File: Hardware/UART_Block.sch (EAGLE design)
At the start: 27 parts, among them U4 TPS62065

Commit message: added DCIN pin added DCIN enable circuit corrected Copper pours corrected name changed names of board and SCH replaced power button updated header footprint added units and cleaned up dimensions
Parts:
- removed R6, R7: 100, SparkFun-Resistors:100OHM1/10W1%(0603)
- added Q1: BSS138, SparkFun-DiscreteSemi:MOSFET-NCHANNELBSS138
- added R15: 1K, SparkFun-Resistors:1KOHM1/10W1%(0603)
- added S2: DPDT, SparkFun-Electromechanical:SWITCH-DPDTAYZ0202
- S1: device SparkFun-Electromechanical:SWITCH-MOMENTARY-2-SMD-1101NE -> SparkFun-Electromechanical:SWITCH-MOMENTARY-2TACTILE-SWITCH-SMD-RIGHT-ANGLE
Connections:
- removed net N$3: R7.1, U1.A1
- removed net N$4: R6.1, U1.A2
- new net DCIN: E1.DCIN, Q1.S, U$3.DCIN
- new net N$1: Q1.G, R15.1
- new net UART1RX: S2.6, U1.B4
- new net UART1TX: S2.3, U1.B3
- new net UART2RX: S2.4, U1.B2
- new net UART2TX: S2.1, U1.B1
- net GND: now also JP2.5, JP2.6; no longer JP2.1, JP2.2
- net GP130_UART_1_RX: now also U1.A4
- net GP131_UART_1_TX: now also U1.A3
- net GP134_UART_2_RX: now also U1.A2; no longer R6.2
- net GP135_UART_2_TX: now also U1.A1; no longer R7.2
- net RXD: now also JP2.2, S2.2; no longer JP2.5, U1.B1
- net TXD: now also JP2.3, S2.5; no longer JP2.4, U1.B2
- net VCC: now also JP2.4, R15.2; no longer JP2.3
- net VSYS: now also Q1.D
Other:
- note added: "Casey Kuhns"
- note added: "DCIN Enable Circuit Prevents Battery board from enabling DCIN"
- note added: "v02"
- moved on the sheet: C1, C10, C2, C8, C9, D3, JP2, L1, R13, R14, R5, R8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

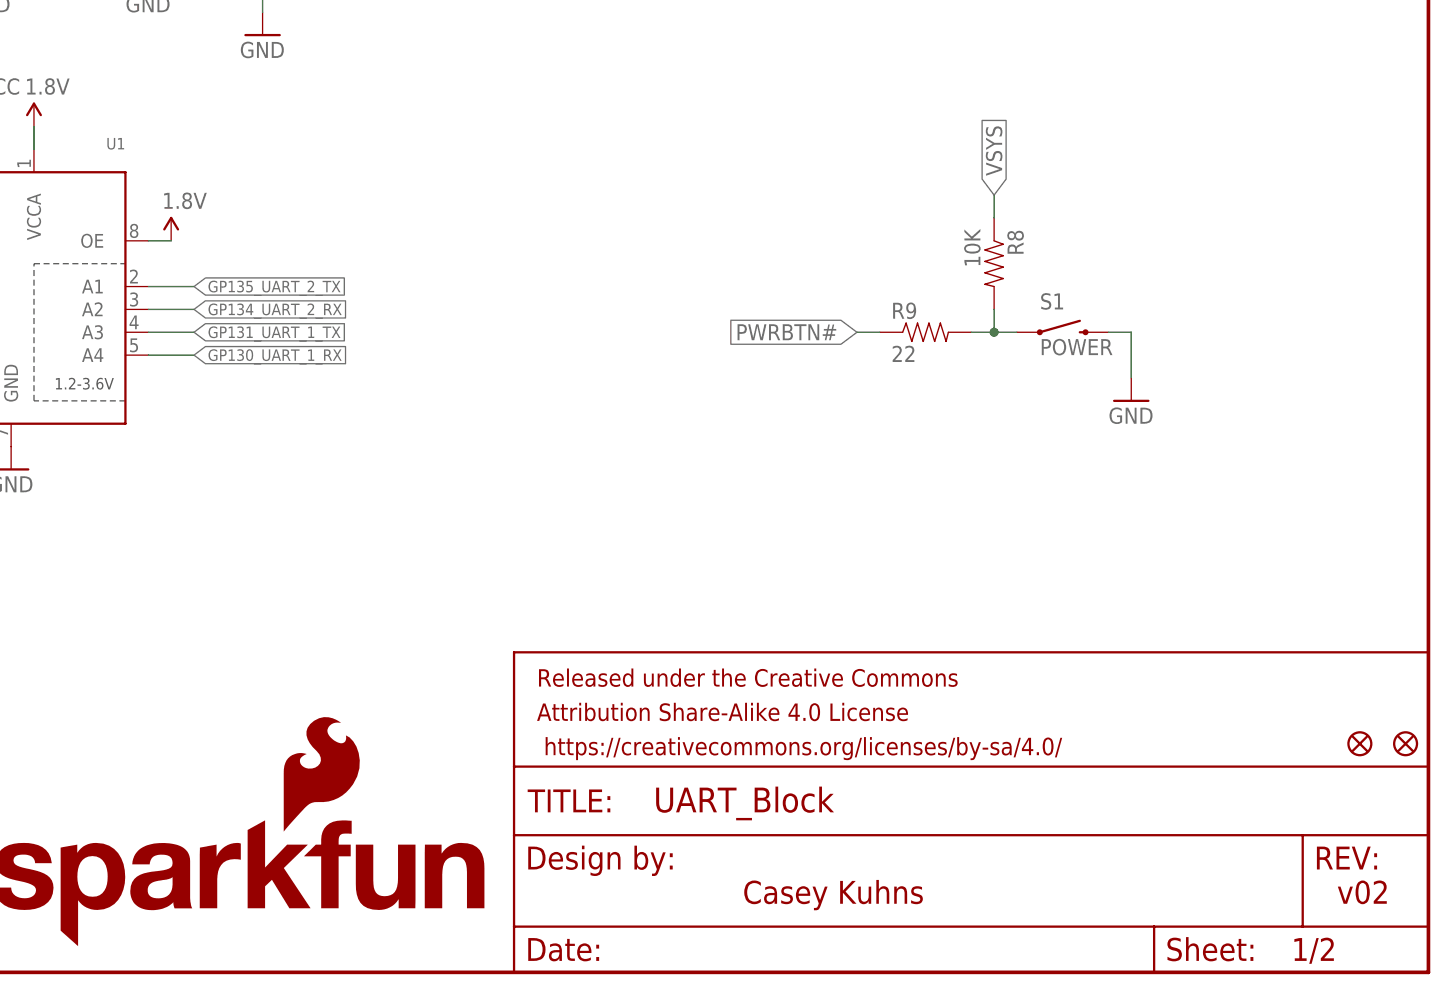
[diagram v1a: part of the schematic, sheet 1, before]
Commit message: Rev to 10, fix gnd, pwr, txt
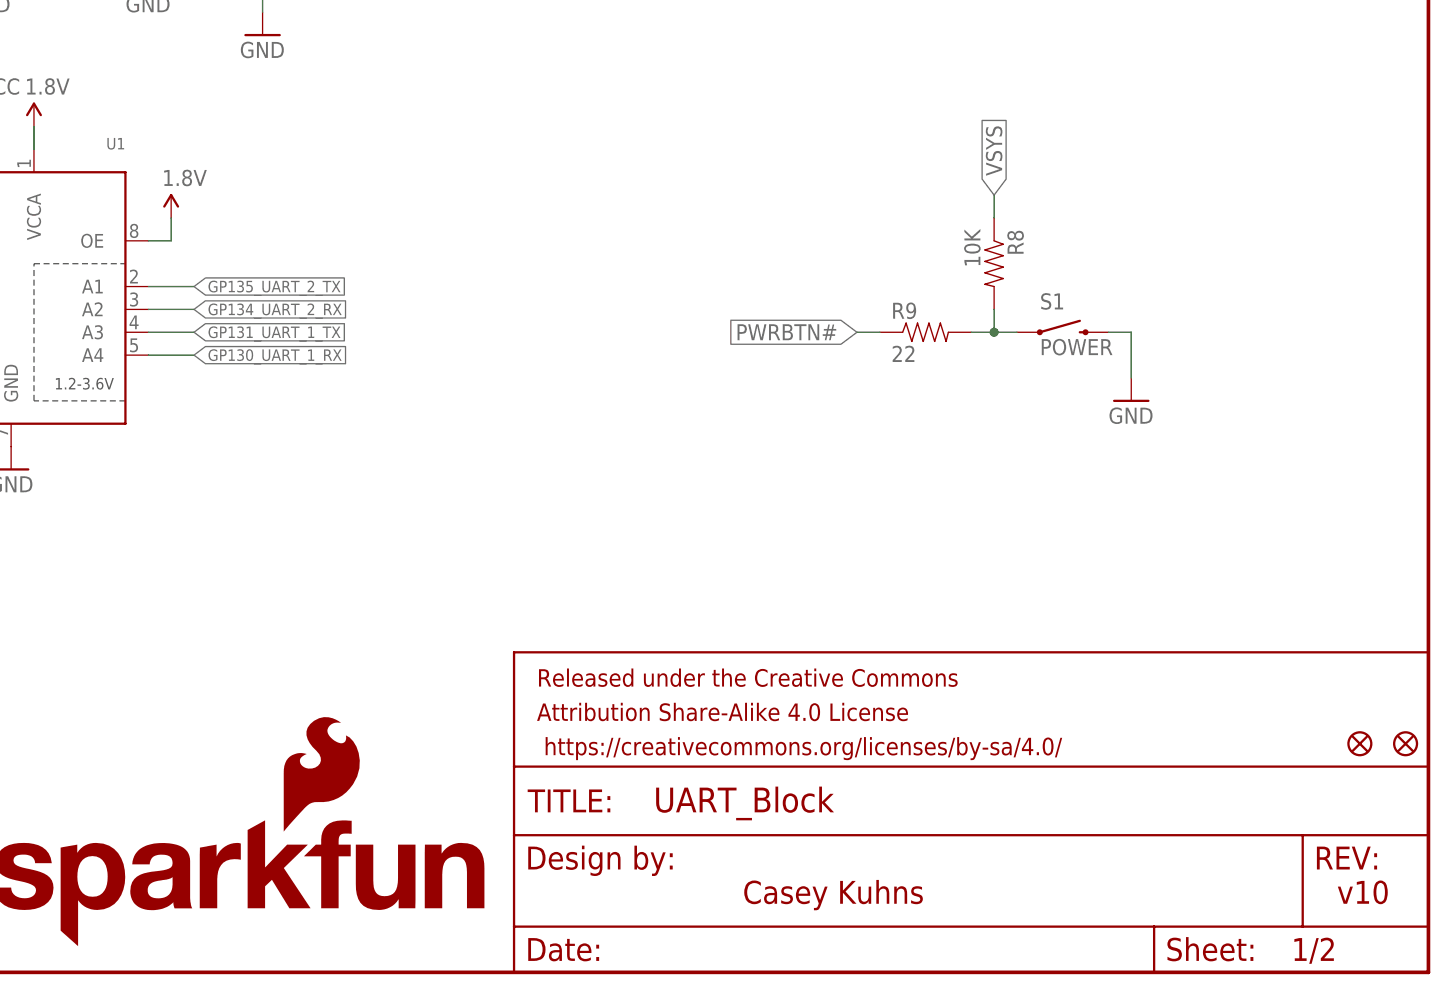
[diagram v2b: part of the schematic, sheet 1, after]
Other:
- note added: "v10"
- note removed: "v02"
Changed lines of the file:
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@@
 <?xml version="1.0" encoding="utf-8"?>
 <!DOCTYPE eagle SYSTEM "eagle.dtd">
-<eagle version="6.5.0">
+<eagle version="6.6.0">
 <drawing>
 <settings>
@@
 <layer number="255" name="routoute" color="7" fill="1" visible="no" active="yes"/>
 </layers>
-<schematic xreflabel="%F%N/%S.%C%R" xrefpart="/%S.%C%R">
+<schematic xreflabel="%F%N/%S" xrefpart="/%S.%C%R">
 <attributes>
 </attributes>
@@
 <text x="35.56" y="78.74" size="1.778" layer="94">Black</text>
 <text x="35.56" y="60.96" size="1.778" layer="94">Green</text>
-<text x="238.76" y="7.62" size="2.54" layer="94">v02</text>
+<text x="238.76" y="7.62" size="2.54" layer="94">v10</text>
 <text x="172.72" y="7.62" size="2.54" layer="94">Casey Kuhns</text>
 <text x="175.26" y="139.7" size="1.27" layer="97">DCIN Enable Circuit
@@
 <instance part="SUPPLY6" gate="G$1" x="20.32" y="76.2"/>
 <instance part="SUPPLY7" gate="G$1" x="22.86" y="137.16"/>
-<instance part="SUPPLY8" gate="G$1" x="109.22" y="81.28"/>
+<instance part="SUPPLY8" gate="G$1" x="109.22" y="83.82"/>
 <instance part="S2" gate="G$1" x="58.42" y="71.12"/>
 <instance part="Q1" gate="G$1" x="195.58" y="127"/>
@@
 <pinref part="U1" gate="G$1" pin="OE"/>
 <wire x1="106.68" y1="81.28" x2="109.22" y2="81.28" width="0.1524" layer="91"/>
+<wire x1="109.22" y1="81.28" x2="109.22" y2="83.82" width="0.1524" layer="91"/>
 <pinref part="SUPPLY8" gate="G$1" pin="1.8V"/>
 </segment>

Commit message: Fix packages, silk, filter cap.
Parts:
- C9: value 9.0pF -> 47pF; device SparkFun-Capacitors:9.0PF-50V-10%(0603) -> SparkFun-Capacitors:47PF-50V-5%(0603)
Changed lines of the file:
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@@
 <part name="R13" library="SparkFun-Resistors" deviceset="RESISTOR" device="0603" value="680k"/>
 <part name="R14" library="SparkFun-Resistors" deviceset="RESISTOR" device="0603" value="120k"/>
-<part name="C9" library="SparkFun-Capacitors" deviceset="9.0PF-50V-10%(0603)" device="" value="9.0pF"/>
+<part name="C9" library="SparkFun-Capacitors" deviceset="47PF-50V-5%(0603)" device="" value="47pF"/>
 <part name="C10" library="SparkFun-Capacitors" deviceset="4.7UF-6.3V-10%(0603)" device="0603" value="4.7uF"/>
 <part name="GND19" library="SparkFun-Aesthetics" deviceset="GND" device=""/>

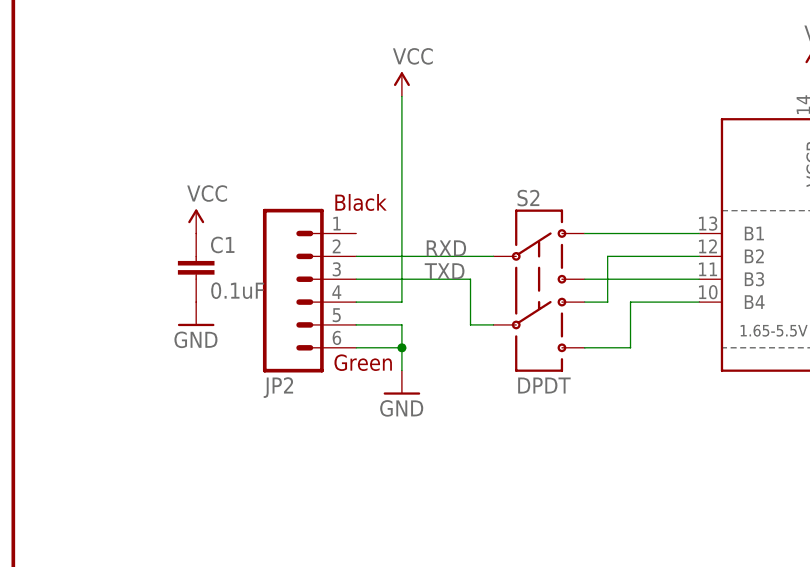
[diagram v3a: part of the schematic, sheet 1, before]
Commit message: Ready for reds Updated and corrected some labels on UART connector. No signal changes. No known to-do items
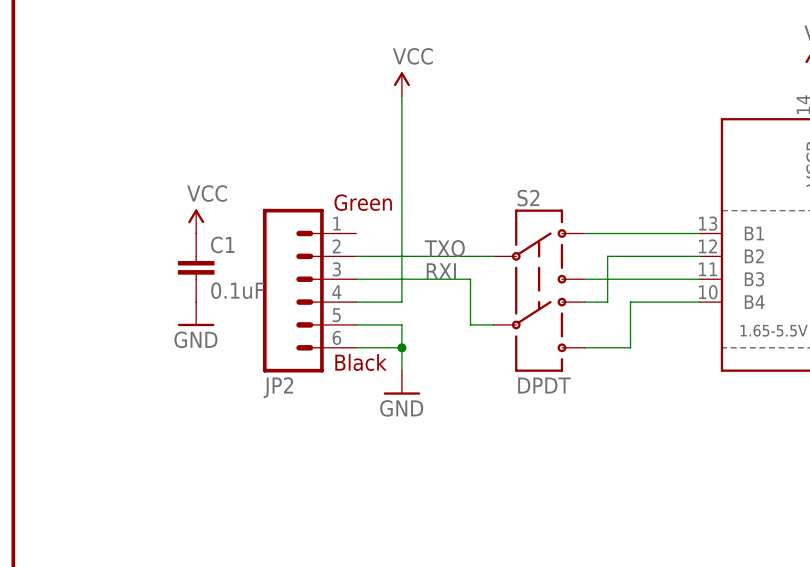
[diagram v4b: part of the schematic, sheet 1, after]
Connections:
- net RXD renamed TXO
- net TXD renamed RXI
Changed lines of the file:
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@@
 <sheet>
 <plain>
-<text x="35.56" y="78.74" size="1.778" layer="94">Black</text>
-<text x="35.56" y="60.96" size="1.778" layer="94">Green</text>
+<text x="35.56" y="60.96" size="1.778" layer="94">Black</text>
+<text x="35.56" y="78.74" size="1.778" layer="94">Green</text>
 <text x="238.76" y="7.62" size="2.54" layer="94">v10</text>
 <text x="172.72" y="7.62" size="2.54" layer="94">Casey Kuhns</text>
@@
 </segment>
 </net>
-<net name="RXD" class="0">
+<net name="TXO" class="0">
 <segment>
 <label x="45.72" y="73.66" size="1.778" layer="95"/>
@@
 </segment>
 </net>
-<net name="TXD" class="0">
+<net name="RXI" class="0">
 <segment>
 <label x="45.72" y="71.12" size="1.778" layer="95"/>

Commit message: added bottom side fids
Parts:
- added FID3, FID4: FIDUCIAL1X2, SparkFun-Aesthetics:FIDUCIAL1X2
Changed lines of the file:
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@@
 <part name="R15" library="SparkFun-Resistors" deviceset="1KOHM1/10W1%(0603)" device="" value="1K"/>
 <part name="SUPPLY9" library="SparkFun-Aesthetics" deviceset="VCC" device=""/>
+<part name="FID3" library="SparkFun-Aesthetics" deviceset="FIDUCIAL" device="1X2"/>
+<part name="FID4" library="SparkFun-Aesthetics" deviceset="FIDUCIAL" device="1X2"/>
 </parts>
 <sheets>
@@
 <instance part="R15" gate="G$1" x="182.88" y="127" rot="R180"/>
 <instance part="SUPPLY9" gate="G$1" x="175.26" y="129.54"/>
+<instance part="FID3" gate="G$1" x="246.38" y="30.48"/>
+<instance part="FID4" gate="G$1" x="241.3" y="30.48"/>
 </instances>
 <busses>
